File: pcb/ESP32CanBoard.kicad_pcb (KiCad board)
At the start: 2 copper layers, 71.1 x 55 mm, 46 parts, among them K1 1Wire, P1 Voltages, P101 CanBus, P2 Power, P3 CONN_1, P4 CONN_1, P5 CONN_1, P6 CONN_1, U1 ESP32Dev, U102 TJA1050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

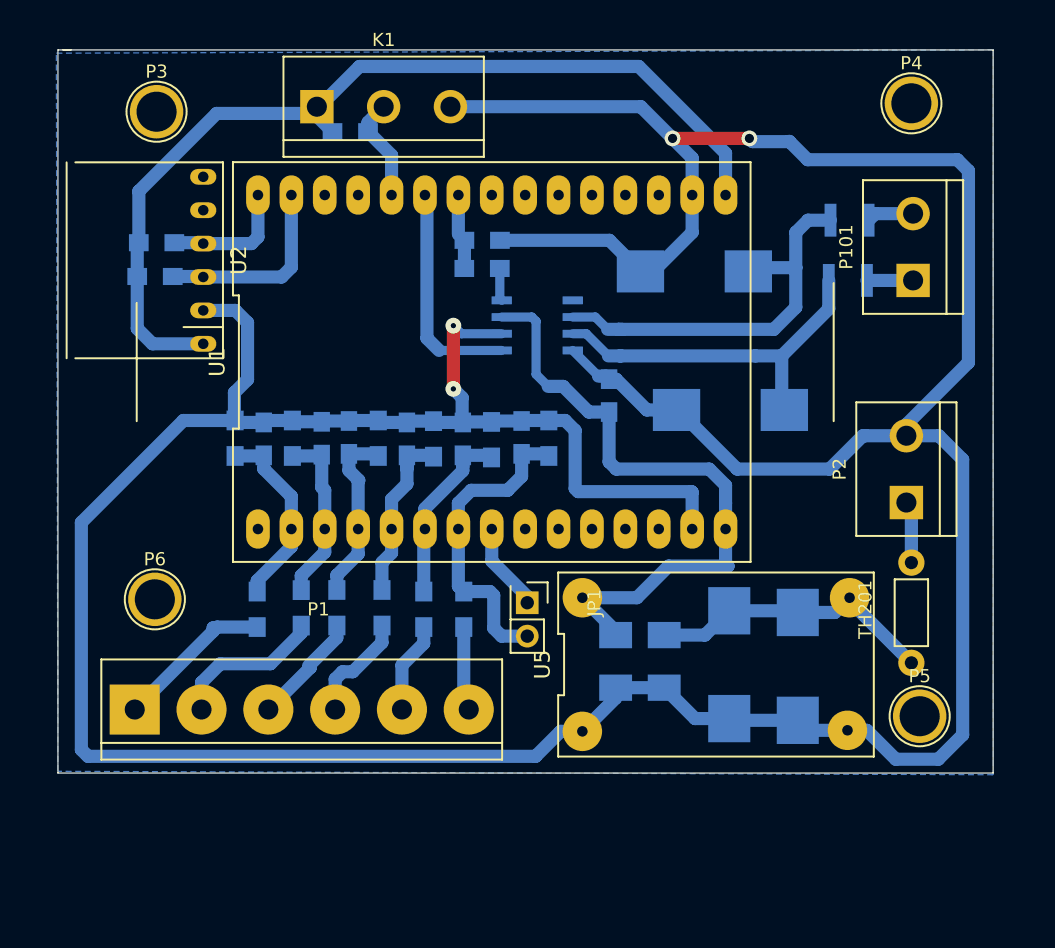
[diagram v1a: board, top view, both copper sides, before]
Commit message: Working version served from flash disk
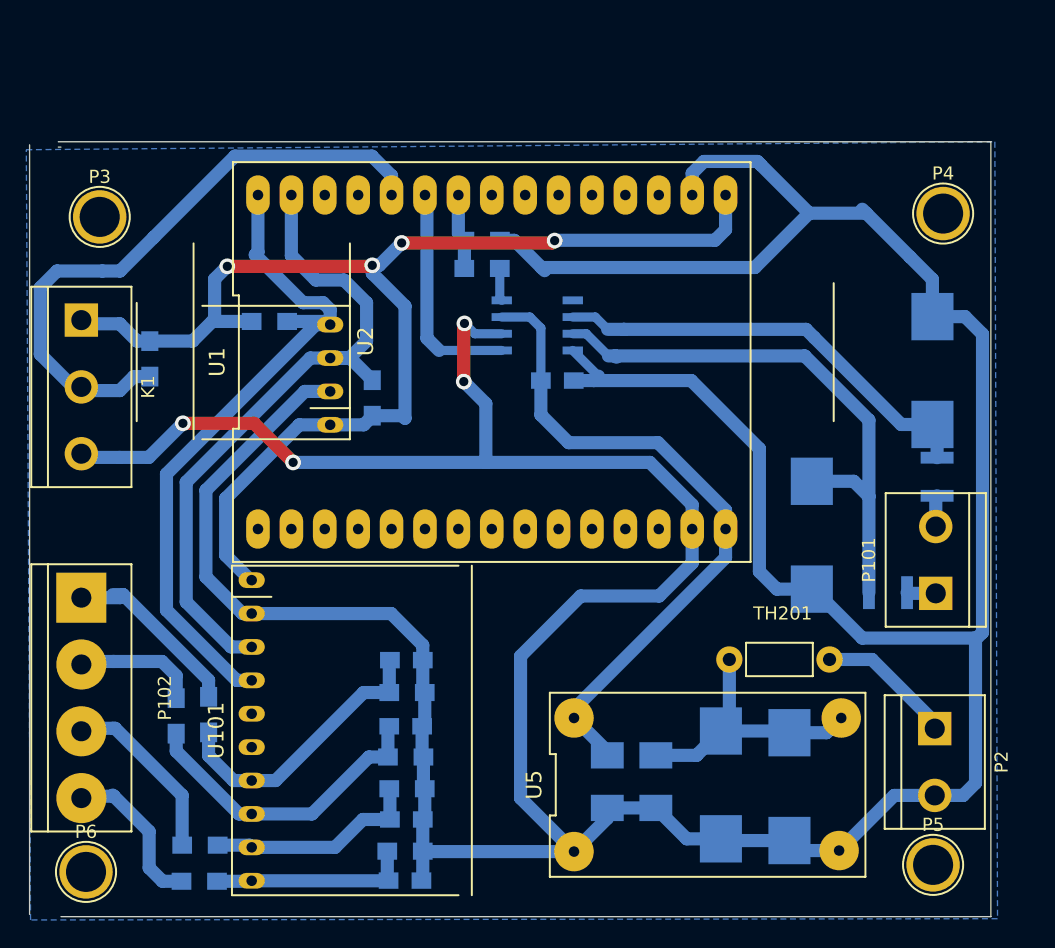
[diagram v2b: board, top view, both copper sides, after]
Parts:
- removed C5, C6: 100nF, Capacitors_SMD:C_0805_HandSoldering
- removed JP1: ADC_CAL, Pin_Headers:Pin_Header_Straight_2x01
- removed P1: Voltages, Connect:bornier6
- removed R12, R13: 1M, Resistors_SMD:R_0805_HandSoldering
- removed R5, R6: 220K, Resistors_SMD:R_0805_HandSoldering
- added P102: CONN_4, Connect:bornier4, F.Cu at (85.1, 107.3)
- added U101: ADS1115, Divers:ADS1115, F.Cu at (96.8, 97.1)
- moved C4 33.6 mm to (109.7, 121.2), turned to 180 degrees
- moved R4 31.4 mm to (109.7, 119.0), turned to 180 degrees
- moved K1 31.3 mm to (85.1, 83.7), turned to 270 degrees
- moved C3 29.4 mm to (109.8, 116.6), turned to 180 degrees
- moved R3 26.7 mm to (109.9, 114.2), turned to 180 degrees
- moved R2 25.7 mm to (109.8, 111.8), turned to 180 degrees
- moved R10 25.0 mm to (94.1, 121.3), turned to 180 degrees
- moved TH1 23.9 mm to (146.4, 99.3)
- moved P101 23.9 mm to (150.1, 96.8)
- moved R1 23.3 mm to (109.9, 106.9), turned to 180 degrees
- moved R11 23.0 mm to (90.3, 81.5), turned to 270 degrees
- moved C2 22.8 mm to (109.8, 109.5), turned to 180 degrees
- moved P2 22.4 mm to (150.0, 112.2), turned to 270 degrees
- moved P6 21.4 mm to (85.4, 120.5)
- moved R9 20.8 mm to (94.1, 118.5), turned to 180 degrees
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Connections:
- C1 pad 2: ADC0 -> Net-(C1-Pad2)
- C2 pad 2: ADC1 -> Net-(C2-Pad2)
- C3 pad 2: ADC2 -> Net-(C3-Pad2)
- C4 pad 2: ADC3 -> Net-(C4-Pad2)
- R1 pad 2: ADC0 -> Net-(C1-Pad2)
- R10 pad 1: ADC3 -> Net-(C4-Pad2)
- R10 pad 2: VIN3 -> Net-(P102-Pad4)
- R2 pad 2: ADC1 -> Net-(C2-Pad2)
- R3 pad 2: ADC2 -> Net-(C3-Pad2)
- R4 pad 2: ADC3 -> Net-(C4-Pad2)
- R7 pad 1: ADC0 -> Net-(C1-Pad2)
- R7 pad 2: VIN0 -> Net-(P102-Pad1)
- R8 pad 1: ADC1 -> Net-(C2-Pad2)
- R8 pad 2: VIN1 -> Net-(P102-Pad2)
- R9 pad 1: ADC2 -> Net-(C3-Pad2)
- R9 pad 2: VIN2 -> Net-(P102-Pad3)
- U1 pad 2: ADC0 -> (no net)
- U1 pad 3: ADC1 -> (no net)
- U1 pad 4: ADC2 -> (no net)
- U1 pad 5: ADC3 -> (no net)
- U1 pad 6: ADC4 -> (no net)
- U1 pad 7: ADC5 -> (no net)
- U1 pad 8: DAC_Calibration -> (no net)
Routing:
- net SDA: track 9.79 -> 52.8 mm
- net 1Wire: track 7.95 -> 47.9 mm
- net SCL: track 14.8 -> 52.3 mm
- net GND: track 315.5 -> 345.4 mm
- net ADC5: track 24.1 -> 0.00 mm
- net 3v3: track 72.8 -> 96.6 mm, vias 0 -> 4
- net Net-(C2-Pad2): track 0.00 -> 23.6 mm
- net Net-(C1-Pad2): track 0.00 -> 21.6 mm
- net Net-(C3-Pad2): track 0.00 -> 16.4 mm
- net ADC4: track 15.7 -> 0.00 mm
- net Net-(C4-Pad2): track 0.00 -> 15.3 mm
- net Net-(D102-Pad2): track 28.1 -> 43.3 mm
- net Net-(P102-Pad1): track 0.00 -> 14.5 mm
- net ADC0: track 14.5 -> 0.00 mm
- net ADC3: track 14.1 -> 0.00 mm
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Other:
- board size 71.1 x 55 mm -> 73.1 x 58.9 mm

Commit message: New board, moved bme280 to CanPressure board
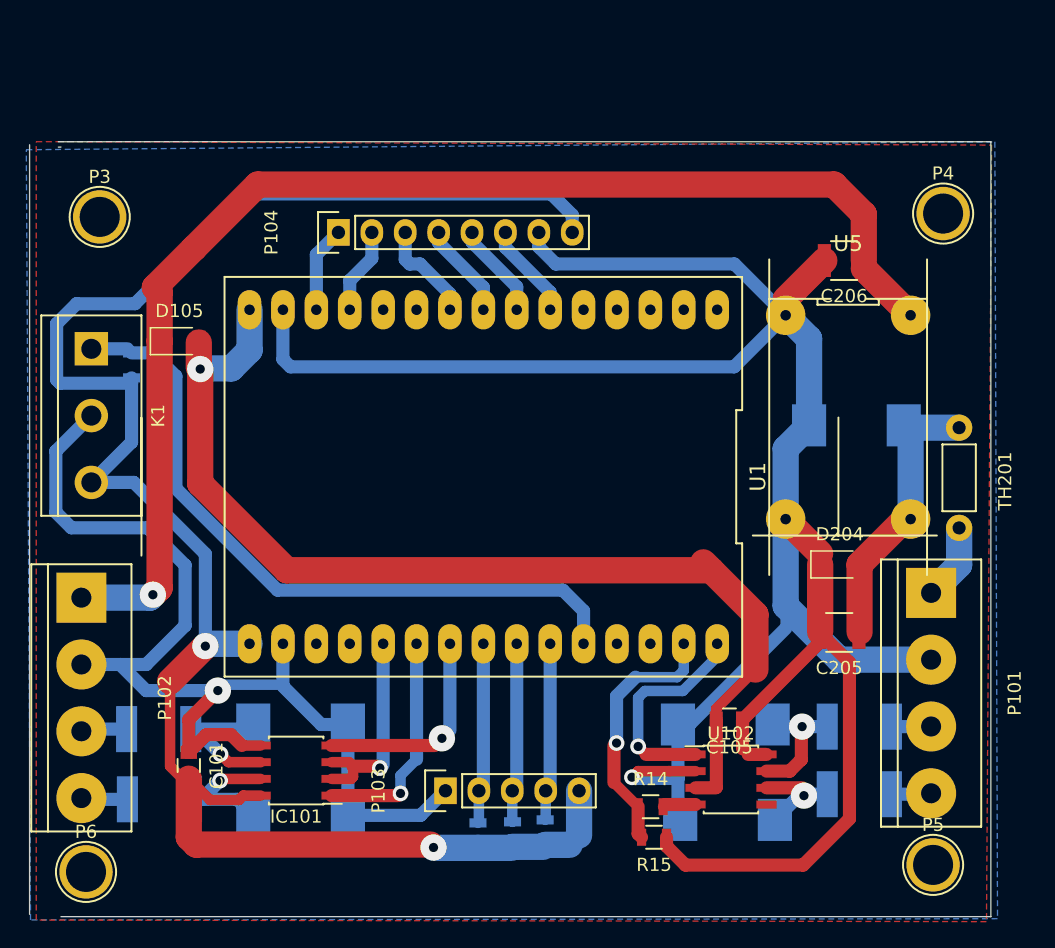
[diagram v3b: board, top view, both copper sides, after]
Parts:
- removed C1, C2, C3, C4: 100nF, Capacitors_SMD:C_0805_HandSoldering
- removed P2: Power, Connect:bornier2
- removed R1, R2, R3, R4: 220K, Resistors_SMD:R_0805_HandSoldering
- removed R10, R7, R8, R9: 1M, Resistors_SMD:R_0805_HandSoldering
- removed U101: ADS1115, Divers:ADS1115
- removed U2: BMP280, Divers:BMP280
- added C101: 100nF, Capacitors_SMD:C_0805, F.Cu at (93.3, 112.5)
- added D103: SMBJ30CA-TR TSV, Diodes_SMD:DO-214AB, B.Cu at (101.8, 116.2)
- added D104: SMBJ30CA-TR TSV, Diodes_SMD:DO-214AB, B.Cu at (101.8, 109.3)
- added D105: 1N5819, Diodes_SMD:D_1206, F.Cu at (92.5, 80.2)
- added IC101: SP3481CN, Housings_SOIC:SOIC-8_3.9x4.9mm_Pitch1.27mm, F.Cu at (101.4, 112.8)
- added P103: Display, Pin_Headers:Pin_Header_Straight_1x05, F.Cu at (112.8, 114.4)
- added P104: Dsiplay, Pin_Headers:Pin_Header_Straight_1x08, F.Cu at (104.6, 71.9)
- added R101: 4K7, Resistors_SMD:R_0805, B.Cu at (120.4, 117.5)
- added TH101: Thermistor, Resistors_SMD:R_1812, B.Cu at (91.0, 109.7)
- added TH102: Thermistor, Resistors_SMD:R_1812, B.Cu at (91.0, 115.0)
- C105: footprint Capacitors_SMD:C_0805_HandSoldering -> Capacitors_SMD:C_0805; moved to F.Cu
- C205, C206: footprint Capacitors_SMD:C_1210_HandSoldering -> Capacitors_SMD:C_1210; moved to F.Cu
- D101, D102, D203: footprint Diodes_SMD:DO-214AB_Handsoldering -> Diodes_SMD:DO-214AB
- D204: footprint Diodes_SMD:DO-214AB_Handsoldering -> Diodes_SMD:D_1206; moved to F.Cu
- P101: value CanBus -> CAN; footprint Connect:bornier2 -> Connect:bornier4
- P102: value CONN_4 -> RS485
- R11, R16, R17: footprint Resistors_SMD:R_0805_HandSoldering -> Resistors_SMD:R_0805
- R14, R15: footprint Resistors_SMD:R_0805_HandSoldering -> Resistors_SMD:R_0805; moved to F.Cu
- TH1, TH2: footprint Resistors_SMD:R_1210 -> Resistors_SMD:R_1812
- U102: moved to F.Cu
- moved R15 47.2 mm to (128.6, 117.9)
- moved C206 43.5 mm to (143.1, 74.1), turned to 180 degrees
- moved R17 43.2 mm to (117.9, 117.7), turned to 90 degrees
- moved R14 42.9 mm to (128.4, 115.6)
- moved D101 37.6 mm to (134.2, 116.6), turned to 0 degrees
- moved U102 37.5 mm to (134.5, 113.5)
- moved R16 34.2 mm to (115.2, 117.8)
- moved U5 29.9 mm to (143.4, 86.0), turned to 270 degrees
- moved C105 28.9 mm to (134.4, 109.0)
- moved D203 27.9 mm to (144.0, 86.6), turned to 0 degrees
- moved TH2 24.9 mm to (144.2, 114.6), turned to 180 degrees
- moved TH201 24.8 mm to (151.8, 86.8), turned to 270 degrees
- moved D204 19.0 mm to (142.8, 97.2), turned to 0 degrees
- moved C205 18.0 mm to (142.7, 102.3), turned to 180 degrees
- moved D102 15.8 mm to (134.1, 109.3), turned to 0 degrees
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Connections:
- C206 pad 1: 5V -> 5.8V
- K1 pad 1: 3v3 -> 1Wire
- K1 pad 2: 1Wire -> GND
- K1 pad 3: GND -> 3v3
- P101 pad 1: Net-(P101-Pad1) -> 12v
- P101 pad 2: Net-(P101-Pad2) -> GND
- P102 pad 1: Net-(P102-Pad1) -> 5.8V
- P102 pad 2: Net-(P102-Pad2) -> GND
- P102 pad 3: Net-(P102-Pad3) -> RS485-A
- P102 pad 4: Net-(P102-Pad4) -> RS485-B
- R11 pad 1: 3v3 -> 1Wire
- R11 pad 2: 1Wire -> 3v3
- TH1 pad 1: Net-(P101-Pad1) -> CAN-H
- TH2 pad 1: Net-(P101-Pad2) -> CAN-L
- U1 pad 12: (no net) -> RST
- U1 pad 13: (no net) -> BL
- U1 pad 20: (no net) -> RS485-EN
- U1 pad 21: (no net) -> RS485-RX
- U1 pad 22: (no net) -> RS485-TX
- U1 pad 23: (no net) -> SCL
- U1 pad 24: CAN-RX -> SDA
- U1 pad 25: CAN-TX -> BTN
- U1 pad 29: SCL -> CAN-RX
- U1 pad 30: SDA -> CAN-TX
- U1 pad 6: (no net) -> MOSI
- U1 pad 7: (no net) -> SCK
- U1 pad 8: (no net) -> CS
- U1 pad 9: (no net) -> DC
- U5 pad 3: 5V -> 5.8V
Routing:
- net 5.8V: track 0.00 -> 101.7 mm, vias 0 -> 1
- net GND: track 345.4 -> 277.4 mm, vias 4 -> 2
- net 3v3: track 96.6 -> 142.5 mm, vias 4 -> 2
- net SDA: track 52.8 -> 13.7 mm
- net SCL: track 52.3 -> 13.8 mm
- net Net-(D102-Pad2): track 43.3 -> 9.77 mm, vias 0 -> 1
- net 5V: track 51.4 -> 81.4 mm, vias 0 -> 1
- net Net-(D101-Pad2): track 33.4 -> 8.53 mm, vias 0 -> 1
- net Net-(C2-Pad2): track 23.6 -> 0.00 mm
- net Net-(C1-Pad2): track 21.6 -> 0.00 mm
- net RS485-RX: track 0.00 -> 17.2 mm, vias 0 -> 1
- net Net-(C3-Pad2): track 16.4 -> 0.00 mm
- net RS485-TX: track 0.00 -> 16.1 mm, vias 0 -> 1
- net RS485-EN: track 0.00 -> 15.9 mm, vias 0 -> 1
- net Net-(C4-Pad2): track 15.3 -> 0.00 mm
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- added copper zone on F.Cu, net GND
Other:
- net class Default: clearance 0.5 -> 0.25; trace_width 1 -> 2; via_dia 1.2 -> 2
- rule trace_clearance: 0.5 -> 0.25
